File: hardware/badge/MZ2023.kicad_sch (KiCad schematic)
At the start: 34 parts, among them J1 Conn_01x04, J10 SAO, J2 Conn_01x04, J3 Conn_01x04, J4 Conn_01x04, J9 SAO, Q2 DMG2301L, U1 Pico

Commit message: PCB Layout
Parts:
- removed C? (x2): C, symbol Device:C
- removed D7, D8: WS2812B, LED_SMD:LED_WS2812B_PLCC4_5.0x5.0mm_P3.2mm, symbol LED:WS2812B
- removed J10, J9: SAO, Connector_PinSocket_2.54mm:PinSocket_2x03_P2.54mm_Vertical_SMD, symbol Connector_Generic:Conn_02x03_Odd_Even
- removed J?: Conn_01x04, Tillo:Grove_SMD, symbol Connector_Generic:Conn_01x04
- removed J?: Conn_01x14_Female, Connector_PinSocket_2.54mm:PinSocket_1x14_P2.54mm_Vertical, symbol Connector:Conn_01x14_Female
- removed J?: Conn_01x04_Female, Connector_PinSocket_2.54mm:PinSocket_1x04_P2.54mm_Vertical, symbol Connector:Conn_01x04_Female
- removed J?: Conn_01x02_Male, symbol Connector:Conn_01x02_Male
- removed U?: BD3571YFP, Package_TO_SOT_SMD:TO-252-2, symbol Regulator_Linear:LF50_TO252
- added C3: 10µ, Capacitor_SMD:C_1206_3216Metric_Pad1.33x1.80mm_HandSolder, symbol Device:C
- added D7: BAT, LED_SMD:LED_0603_1608Metric_Pad1.05x0.95mm_HandSolder, symbol Device:LED
- added J5: Conn_01x08_Female, Connector_PinSocket_2.54mm:PinSocket_1x08_P2.54mm_Vertical_SMD_Pin1Right, symbol Connector:Conn_01x08_Female
- added J6: Conn_01x02_Male, Connector_JST:JST_PH_S2B-PH-K_1x02_P2.00mm_Horizontal, symbol Connector:Conn_01x02_Male
- added R5, R6: 1k, Resistor_SMD:R_0805_2012Metric_Pad1.20x1.40mm_HandSolder, symbol Device:R
- added SW4: SW_Push_SPDT, Button_Switch_THT:SW_CuK_OS102011MA1QN1_SPDT_Angled, symbol Switch:SW_Push_SPDT
- added TP2, TP3, TP5, TP6, TP7: NP, TestPoint:TestPoint_Keystone_5015_Micro-Minature, symbol Connector:TestPoint
- added U3: MCP73831-2-OT, Package_TO_SOT_SMD:SOT-23-5, symbol Battery_Management:MCP73831-2-OT
- D10: renamed from D?; footprint (none) -> Diode_SMD:D_MiniMELF
- SW1, SW2, SW3: renamed from SW?; footprint Button_Switch_SMD:SW_SPST_Omron_B3FS-105xP -> Button_Switch_SMD:SW_Push_1P1T_NO_CK_KMR2
- gave numbers to parts that had none: 5
- renumbered TP5 to TP1
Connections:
- net +3V3: now also J5.1 (Pin_1)
- net GND: now also C3.2, J5.2 (Pin_2), J6.2 (Pin_2), R5.2, U3.2 (VSS)
- net GP10: now also J5.8 (Pin_8)
- net GP11: now also J5.7 (Pin_7)
- net GP12: now also J5.4 (Pin_4)
- net GP13: now also J5.5 (Pin_5)
- net GP14: now also J5.6 (Pin_6)
- net GP16: now also TP7.1; no longer R3.1
- net GP17: now also TP6.1
- net GP18: now also TP5.1
- net GP19: now also TP4.1
- net GP20: now also TP3.1
- net GP21: now also TP2.1
- net GP28: now also J5.3 (Pin_3)
- net VBUS: now also D7.2 (A), U3.4 (VDD)
- net VCC: now also SW4.1 (A); no longer U1.39 (VSYS)
- net GP8: now reaches U1.11 (GPIO8)
- net GP8: now also R3.1; no longer TP4.1
- net +BATT: now reaches Q2.2 (S)
- net +BATT: now also C3.1, J6.1 (Pin_1), U3.3 (VBAT)
- new net: R5.1, U3.5 (PROG)
- new net: SW4.2 (B), U1.39 (VSYS)
- new net: D7.1 (K), R6.1
- new net: R6.2, U3.1 (STAT)
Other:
- note added: "ADC2 (SAO)"
- note added: "Battery: Lipo, standard solution from adafruit feathers"
- note added: "Cheap China color TFT, and cover connection"
- note added: "SPI1 (TFT) SAO"
- note added: "tft_cs = board.GP28 tft_res = board.GP12 tft_dc = board.GP13 tft_mosi = board.GP11 tft_clk = board.GP14 tft_led = board.GP10"
- note removed: "(ADC0) (ADC1)"
- note removed: "(SAO)"
- note removed: "ADC2"
- note removed: "Battery: 9V, rechargeable over USB. like last year."
- note removed: "Cheap China color TFT"
- note removed: "Connection to the cover"
- note removed: "SAO"
- note removed: "SAO IO"
- note removed: "SPI1 (TFT)"
- note removed: "tft_cs = board.GP11 tft_res = board.GP12 tft_dc = board.GP13 spi_mosi = board.GP15 spi_clk = board.GP14"
- moved on the sheet: Q2, R4, SW3

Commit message: prototype
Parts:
- removed TP1, TP2, TP3, TP4, TP5, TP6, TP7: NP, TestPoint:TestPoint_Keystone_5015_Micro-Minature, symbol Connector:TestPoint
- added J7: Conn_01x07_Female, Connector_PinSocket_2.54mm:PinSocket_1x07_P2.54mm_Vertical_SMD_Pin1Right, symbol Connector:Conn_01x07_Female
- D9: footprint LED_SMD:LED_0603_1608Metric_Pad1.05x0.95mm_HandSolder -> LED_SMD:LED_1206_3216Metric_ReverseMount_Hole1.8x2.4mm
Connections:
- net GP16: now also J7.2 (Pin_2)
- net GP17: now also J7.3 (Pin_3)
- net GP18: now also J7.4 (Pin_4)
- net GP19: now also J7.5 (Pin_5)
- net GP20: now also J7.6 (Pin_6)
- net GP21: now also J7.7 (Pin_7)
- net GP9: now reaches U1.12 (GPIO9)
- net GP9: now also J7.1 (Pin_1)

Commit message: WIP
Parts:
- removed D9: LED, LED_SMD:LED_1206_3216Metric_ReverseMount_Hole1.8x2.4mm, symbol Device:LED
- added D?: LED, LED_SMD:LED_0603_1608Metric_Pad1.05x0.95mm_HandSolder, symbol Device:LED
- D1, D2, D3, D4, D5, D6: Digikey (none) -> 1568-COM-16347CT-ND; LCSC (none) -> C114586
- D10: value D -> LL4448 L1G; Digikey (none) -> LL4448L1GCT-ND; LCSC (none) -> C183025; Mouser (none) -> 78-LL4154
- J6: Digikey (none) -> 455-1719-ND; LCSC (none) -> C157932
- Q2: Digitec (none) -> DMG2301L-7DICT-ND; LCSC (none) -> C102619; Mouser (none) -> 621-DMG2301L-7
- SW1, SW2, SW3: Digikey (none) -> CKN10244CT-ND; LCSC (none) -> C269272; Mouser (none) -> 611-KMR221NGLFS
- SW4: Digikey (none) -> CKN9559-ND; LCSC (none) -> C226259; Mouser (none) -> 611-OS102011MA1QN1
- U3: Digikey (none) -> MCP73831T-2ACI/OT; LCSC (none) -> C424093; Mouser (none) -> 579-MCP73831T-2ACIOT
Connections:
- net GND: now also D?.1 (K)
- net at R3.2: now also D?.2 (A)
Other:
- note added: "(Order seperately)"
- note added: "Raspi Pico W"
- company: (none) -> Make Zürich
- title: (none) -> MZ 2023 badge
- moved on the sheet: C3, D1, D10, D2, D3, D4, D5, D6, D7, J1, J2, J3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

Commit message: some parts anotated
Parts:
- gave numbers to parts that had none: 1
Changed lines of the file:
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@@
   (symbol (lib_id "Device:LED") (at 99.695 172.085 90) (unit 1)
     (in_bom yes) (on_board yes)
-    (property "Reference" "D?" (id 0) (at 94.615 172.085 90)
+    (property "Reference" "D8" (id 0) (at 94.615 172.085 90)
       (effects (font (size 1.27 1.27)) (justify right))
     )
@@
       (reference "D7") (unit 1) (value "BAT") (footprint "LED_SMD:LED_0603_1608Metric_Pad1.05x0.95mm_HandSolder")
     )
+    (path "/4f8c9628-c750-4e20-82cf-aa0b1a8148d0"
+      (reference "D8") (unit 1) (value "LED") (footprint "LED_SMD:LED_0603_1608Metric_Pad1.05x0.95mm_HandSolder")
+    )
     (path "/b73d2bff-4e30-4a85-84b9-cfb8c50036f7"
       (reference "D10") (unit 1) (value "LL4448 L1G") (footprint "Diode_SMD:D_MiniMELF")
     )
-    (path "/4f8c9628-c750-4e20-82cf-aa0b1a8148d0"
-      (reference "D?") (unit 1) (value "LED") (footprint "LED_SMD:LED_0603_1608Metric_Pad1.05x0.95mm_HandSolder")
-    )
     (path "/c9f9dc46-8393-47e9-87a9-e5f3507d1f5d"

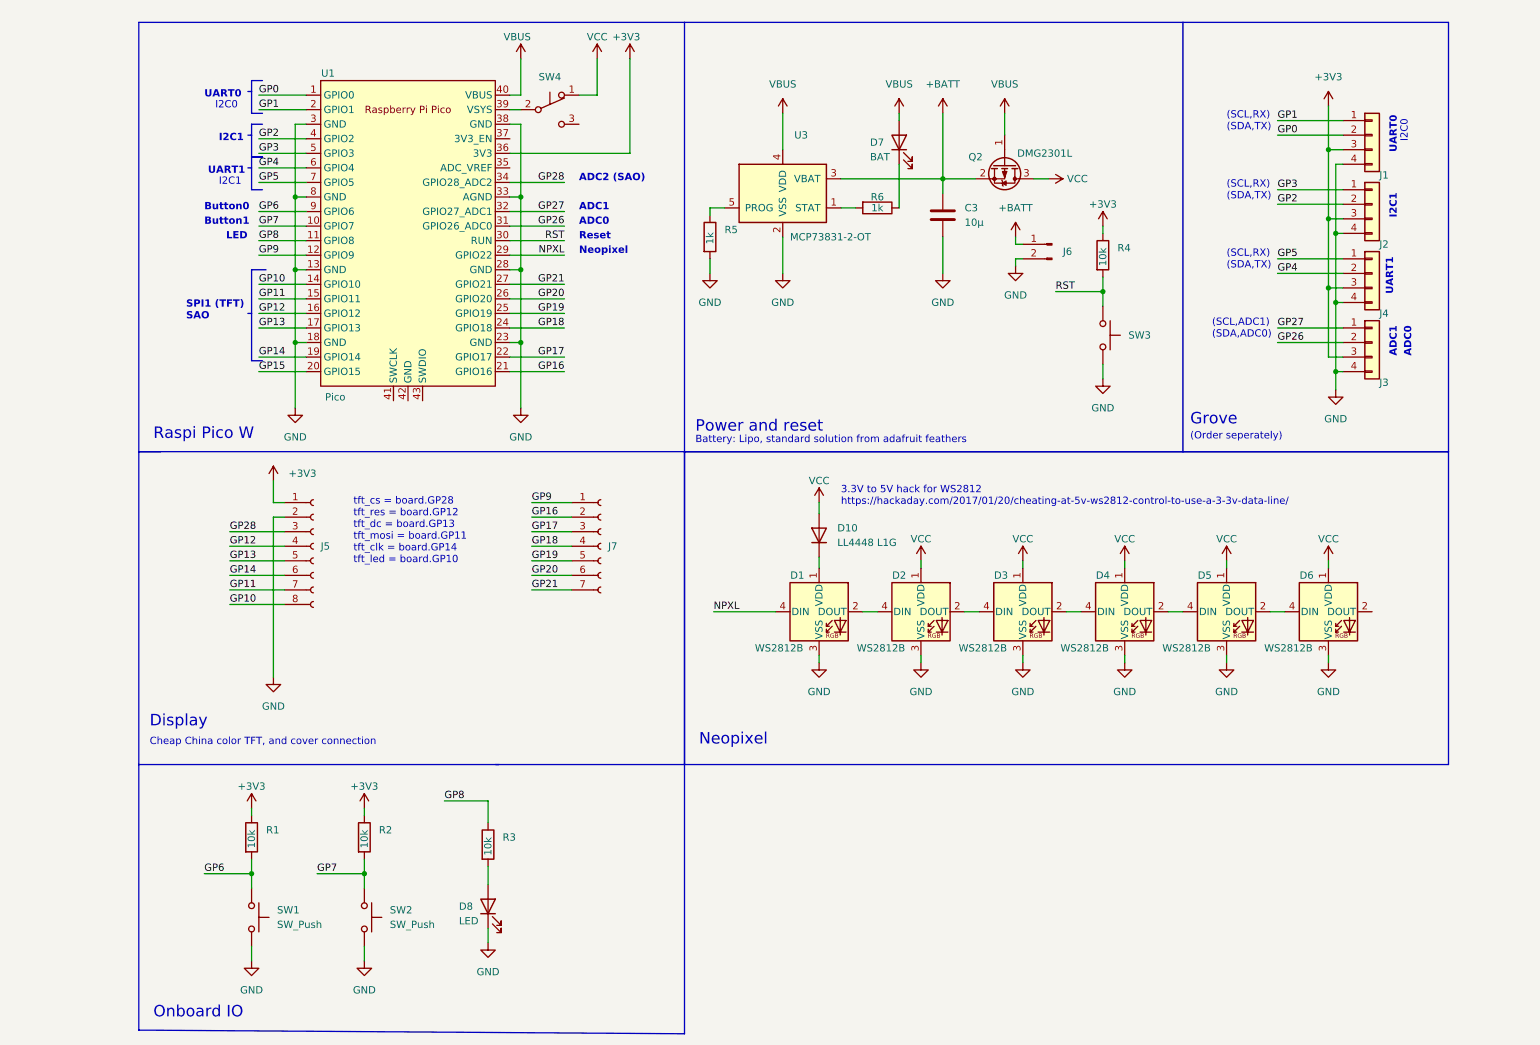
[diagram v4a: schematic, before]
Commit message: new version: * added Seeed Studio LoRa e5 module * changed WS2812 LED from 5x5mm to 3.5x3.5mm footprint * changed WS2812 LED positions. From circle to "rectangular" with intention of becoming the top cover backlight * 2 Groove connectors (J3 and J4) removed from top and moved to bottom * Groove J4 connector now connected to GP20 and GP21 (previously GP4 and GP5) * Removed GP20 and GP21 from J7 pin header (the one on the left, 5 pins) * Added one extra GND and VCC pins to the connector J5 (the one on the right, 10 pins) * removed SW2 * SW4 (ON/OFF) moved on top * WS2812 takes power from VCC (either 5V from USB or the battery voltage * MCP73831 prog current set to 500mAh, fixed LED charging status
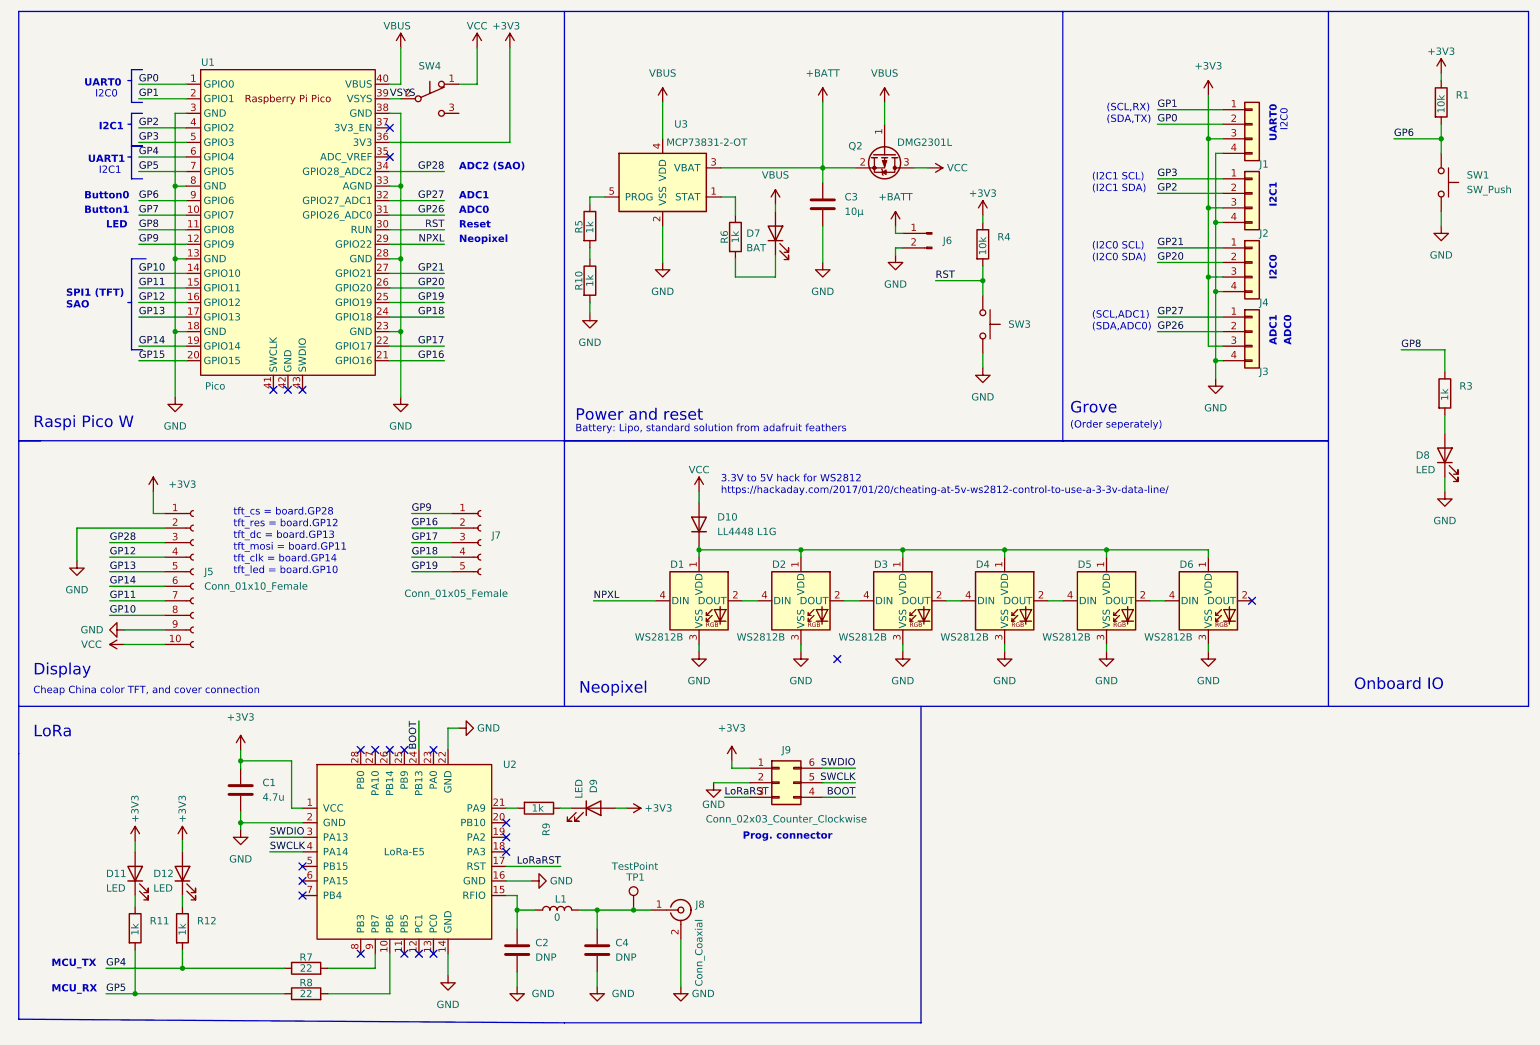
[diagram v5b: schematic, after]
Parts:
- removed J5: Conn_01x08_Female, Connector_PinSocket_2.54mm:PinSocket_1x08_P2.54mm_Vertical_SMD_Pin1Right, symbol Connector:Conn_01x08_Female
- removed J7: Conn_01x07_Female, Connector_PinSocket_2.54mm:PinSocket_1x07_P2.54mm_Vertical_SMD_Pin1Right, symbol Connector:Conn_01x07_Female
- removed R2: 10k, Resistor_SMD:R_0805_2012Metric_Pad1.20x1.40mm_HandSolder, symbol Device:R
- removed SW2: SW_Push, Button_Switch_SMD:SW_Push_1P1T_NO_CK_KMR2, symbol Switch:SW_Push
- added C1: 4.7u, Capacitor_SMD:C_0603_1608Metric, symbol Device:C
- added C2, C4: DNP, Capacitor_SMD:C_0603_1608Metric, symbol Device:C
- added D11, D12, D9: LED, LED_SMD:LED_0603_1608Metric_Pad1.05x0.95mm_HandSolder, symbol Device:LED
- added J5: Conn_01x10_Female, Connector_PinHeader_2.54mm:PinHeader_1x10_P2.54mm_Vertical, symbol Connector:Conn_01x10_Female
- added J7: Conn_01x05_Female, Connector_PinHeader_2.54mm:PinHeader_1x05_P2.54mm_Vertical, symbol Connector:Conn_01x05_Female
- added J8: Conn_Coaxial, Connector_Coaxial:U.FL_Hirose_U.FL-R-SMT-1_Vertical, symbol Connector:Conn_Coaxial
- added J9: Conn_02x03_Counter_Clockwise, Connector_PinHeader_2.54mm:PinHeader_2x03_P2.54mm_Vertical_SMD, symbol Connector_Generic:Conn_02x03_Counter_Clockwise
- added L1: 0, Inductor_SMD:L_0805_2012Metric_Pad1.15x1.40mm_HandSolder, symbol Device:L
- added R10, R11, R12, R9: 1k, Resistor_SMD:R_0603_1608Metric, symbol Device:R
- added R7, R8: 22, Resistor_SMD:R_0603_1608Metric, symbol Device:R
- added TP1: TestPoint, Connector_PinHeader_2.54mm:PinHeader_1x01_P2.54mm_Vertical, symbol Connector:TestPoint
- added U2: LoRa-E5, LoRa-E5:LoRa-E5, symbol LoRa-E5:LoRa-E5
- D1, D2, D3, D4, D5, D6: footprint LED_SMD:LED_WS2812B_PLCC4_5.0x5.0mm_P3.2mm -> LED_SMD:LED_SK6812MINI_PLCC4_3.5x3.5mm_P1.75mm
- R1, R4, R5, R6: footprint Resistor_SMD:R_0805_2012Metric_Pad1.20x1.40mm_HandSolder -> Resistor_SMD:R_0603_1608Metric
- R3: value 10k -> 1k; footprint Resistor_SMD:R_0805_2012Metric_Pad1.20x1.40mm_HandSolder -> Resistor_SMD:R_0603_1608Metric
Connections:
- net +3V3: now also C1.1, D11.2 (A), D12.2 (A), D9.2 (A), J5.1 (Pin_1), J9.1 (Pin_1), U2.1 (VCC)
- net GND: now also C1.2, C2.2, C4.2, J5.2 (Pin_2), J5.9 (Pin_9), J8.2 (Ext), J9.2 (Pin_2), R10.2, U2.14 (GND), U2.16 (GND), U2.2 (GND), U2.22 (GND); no longer R5.2
- net GP10: now also J5.8 (Pin_8)
- net GP11: now also J5.7 (Pin_7)
- net GP12: now also J5.4 (Pin_4)
- net GP13: now also J5.5 (Pin_5)
- net GP14: now also J5.6 (Pin_6)
- net GP16: now also J7.2 (Pin_2)
- net GP17: now also J7.3 (Pin_3)
- net GP18: now also J7.4 (Pin_4)
- net GP19: now also J7.5 (Pin_5)
- net GP20: now also J4.2 (Pin_2)
- net GP21: now also J4.1 (Pin_1)
- net GP28: now also J5.3 (Pin_3)
- net GP4: now also R12.2, R7.1; no longer J4.2 (Pin_2)
- net GP5: now also R11.2, R8.1; no longer J4.1 (Pin_1)
- net GP9: now also J7.1 (Pin_1)
- net VCC: now also J5.10 (Pin_10); no longer D2.1 (VDD), D3.1 (VDD), D4.1 (VDD), D5.1 (VDD), D6.1 (VDD)
- net VSYS: now reaches SW4.2 (B), U1.39 (VSYS)
- net at R6.1: now also U3.1 (STAT); no longer D7.1 (K)
- net at R6.2: now also D7.1 (K); no longer U3.1 (STAT)
- net at D1.1 (VDD), D10.1 (K): now also D2.1 (VDD), D3.1 (VDD), D4.1 (VDD), D5.1 (VDD), D6.1 (VDD)
- new net: D9.1 (K), R9.1
- new net: R10.1, R5.2
- new net: R8.2, U2.10 (PB6)
- new net: C2.1, L1.1, U2.15 (RFIO)
- new net: R9.2, U2.21 (PA9)
- new net: R7.2, U2.9 (PB7)
- new net: C4.1, J8.1 (In), L1.2, TP1.1
- new net: D12.1 (K), R12.1
- new net: D11.1 (K), R11.1
- new net BOOT: J9.4 (Pin_4), U2.24 (PB13~{})
- new net LoRaRST: J9.3 (Pin_3), U2.17 (RST)
- new net SWCLK: J9.5 (Pin_5), U2.4 (PA14)
- new net SWDIO: J9.6 (Pin_6), U2.3 (PA13)
- no-connect marks 0 -> 22
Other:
- note added: "(I2C0 SCL) (I2C0 SDA)"
- note added: "(I2C1 SCL) (I2C1 SDA)"
- note added: "LoRa"
- note added: "MCU_RX"
- note added: "MCU_TX"
- note added: "Prog. connector"
- moved on the sheet: C3, D1, D10, D2, D3, D4, D5, D6, D7, D8, J1, J2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

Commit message: lora e5 v0.2 * changed grove connectors to right angle version * changed footprint for RDB LEDs WS2812B -> SK6812MINI (compatible with NeoPixels * mechanical switch (SW4) now cut the BAT+ instead of VCC (VSYS) * move lipo charging circuit to free space for new grove connectors and MKZH logo * created MakeZurich logo * improved silk
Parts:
- C1: footprint Capacitor_SMD:C_0603_1608Metric -> Capacitor_SMD:C_0805_2012Metric
- D1, D2, D3, D4, D5, D6: value WS2812B -> SK6812MINI; symbol LED:WS2812B -> LED:SK6812MINI; Digikey 1568-COM-16347CT-ND -> (none); LCSC C114586 -> (none)
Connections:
- net +BATT: now also SW4.1 (A); no longer C3.1, Q2.2 (S), U3.3 (VBAT)
- net GND: now also D1.2 (VSS), D2.2 (VSS), D3.2 (VSS), D4.2 (VSS), D5.2 (VSS), D6.2 (VSS); no longer D1.3 (VSS), D2.3 (VSS), D3.3 (VSS), D4.3 (VSS), D5.3 (VSS), D6.3 (VSS)
- net NPXL: now also D1.3 (DIN); no longer D1.4 (DIN)
- net VCC: now also U1.39 (VSYS); no longer SW4.1 (A)
- net at D6.4 (VDD): now also D1.4 (VDD), D10.1 (K), D2.4 (VDD), D3.4 (VDD), D4.4 (VDD), D5.4 (VDD); no longer D5.2 (DOUT)
- net GP15: no longer names the net of U1.20 (GPIO15)
- net GP7: no longer names the net of U1.10 (GPIO7)
- net VSYS renamed VBAT
- net VBAT: now also C3.1, Q2.2 (S), U3.3 (VBAT); no longer U1.39 (VSYS)
- new net: D5.1 (DOUT), D6.3 (DIN)
- new net: D2.1 (DOUT), D3.3 (DIN)
- new net: D1.1 (DOUT), D2.3 (DIN)
- new net: D4.1 (DOUT), D5.3 (DIN)
- new net: D3.1 (DOUT), D4.3 (DIN)
- now unconnected: D6.1 (VDD)
- no-connect marks 22 -> 24
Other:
- note removed: "Button1"
- moved on the sheet: SW4
